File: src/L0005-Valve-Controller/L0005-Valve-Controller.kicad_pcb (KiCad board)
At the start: 4 copper layers, 101 parts, among them J1 Jumper_NO, J2 Jumper_NO, K1 AQH0223AX, K2 AQH0223AX, K3 AQH0223AX, K4 AQH0223AX, K5 AQH0223AX, K6 AQH0223AX, P1 3220-20-0200-00, P10 353620650, P11 353620650, P12 353620650, P13 353620650, P14 647676-3, P15 647676-3, P16 647676-2, P2 140-504-415-000, P3 647676-3, P4 647676-3, P5 647676-3, P6 647676-3, P7 647676-3, P8 647676-3, P9 647676-2, U1 LPC54113J256BD64QL, U2 LMS8117AMP-3.3_NOPB, U3 MAX3370EXK+T, U4 MAX3370EXK+T, U5 Optocoupler

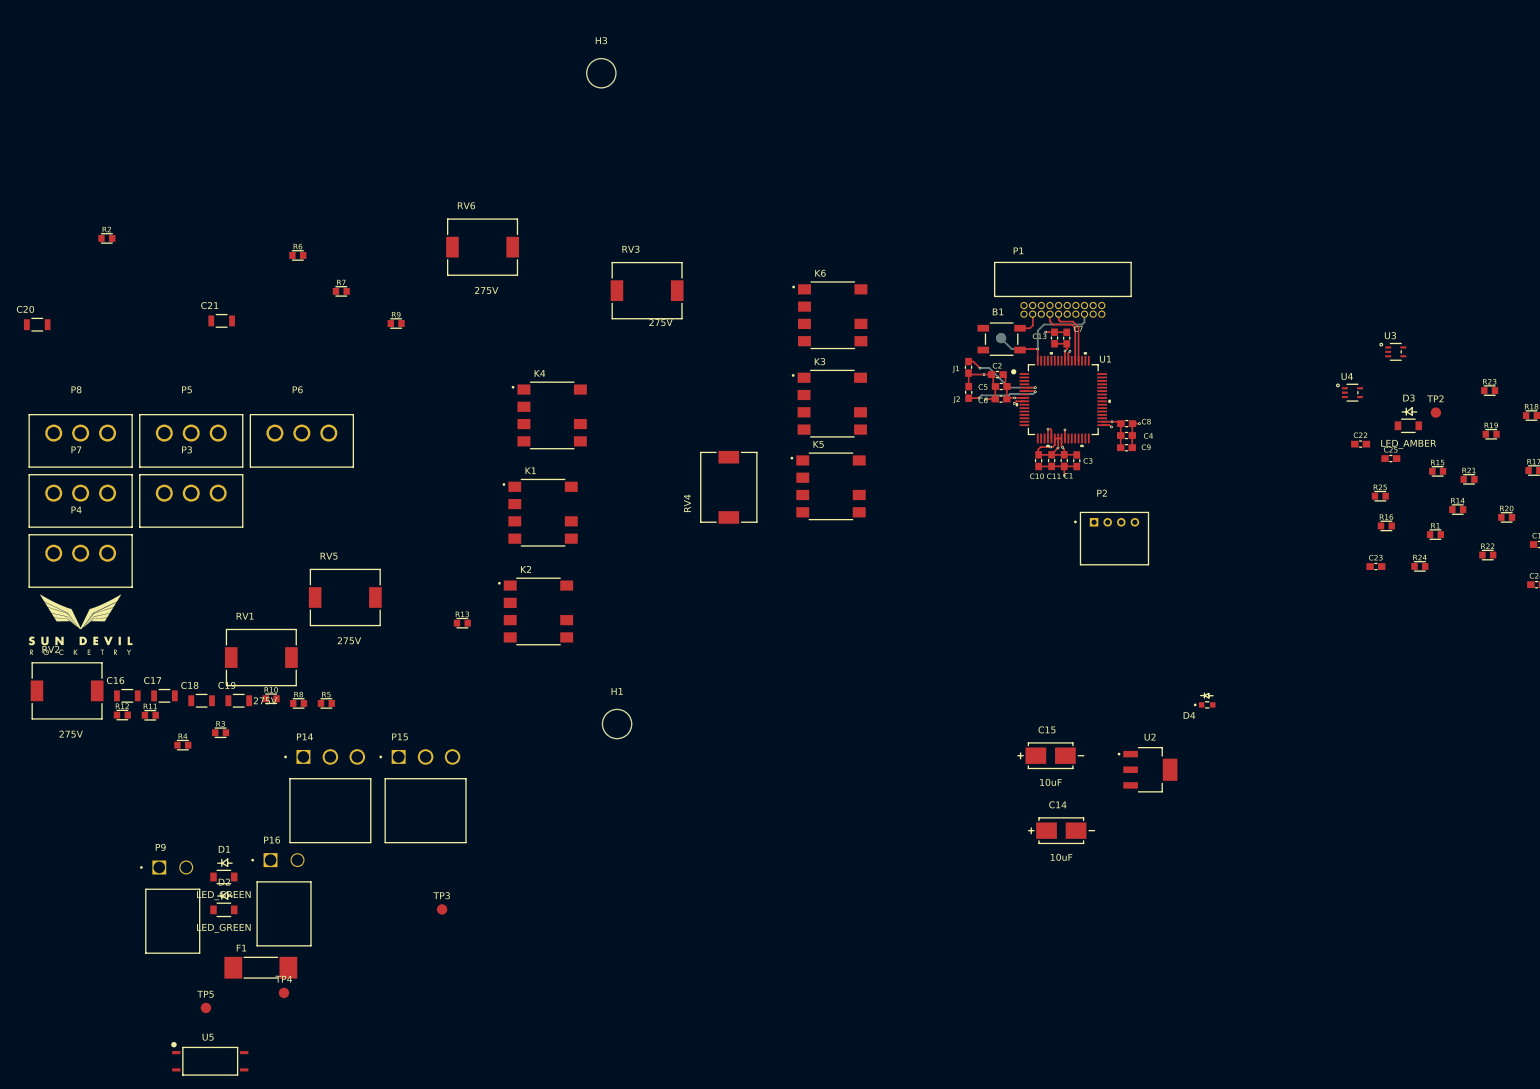
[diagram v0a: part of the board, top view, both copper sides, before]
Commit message: routed solenoid SSRs
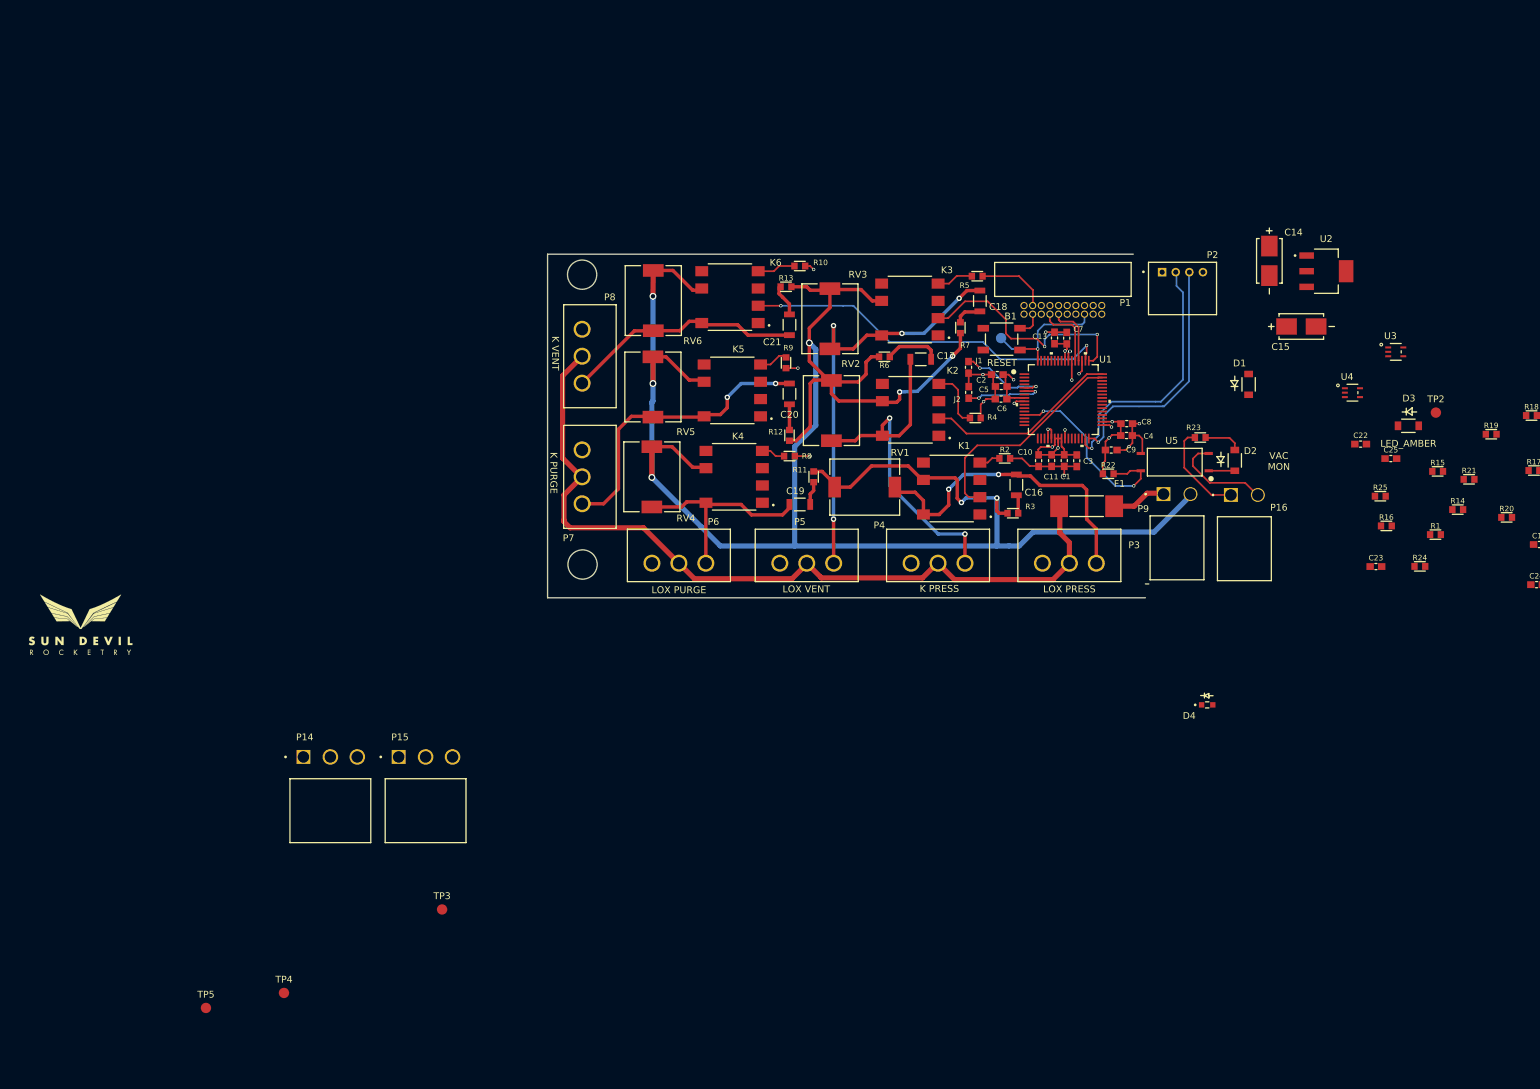
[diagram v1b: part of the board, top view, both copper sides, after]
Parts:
- moved D1 167.1 mm to (160.0, 96.1), turned to 90 degrees
- moved U5 166.9 mm to (149.1, 107.6), turned to 180 degrees
- moved D2 162.6 mm to (157.9, 107.3), turned to 90 degrees
- moved P9 157.5 mm to (147.4, 112.3)
- moved P16 151.0 mm to (157.4, 112.4)
- moved F1 139.1 mm to (136.1, 114.0)
- moved R2 135.9 mm to (124.1, 107.0)
- moved C16 134.3 mm to (125.8, 110.9), turned to 90 degrees
- moved P3 129.5 mm to (133.6, 122.4), turned to 180 degrees
- moved C18 128.6 mm to (120.4, 83.9), turned to 90 degrees
- moved P4 126.1 mm to (114.3, 122.4), turned to 180 degrees
- moved R4 126.0 mm to (119.8, 101.1)
- moved C17 121.7 mm to (111.8, 92.5), turned to 180 degrees
- moved R3 120.9 mm to (125.3, 115.1), turned to 180 degrees
- moved RV2 119.7 mm to (98.6, 100.0), turned to 90 degrees
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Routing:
- net AC_NEUTRAL: track 0.00 -> 309.0 mm, vias 0 -> 8
- net AC_HOT: track 0.00 -> 119.9 mm
- net Net-(C18-Pad2): track 0.00 -> 63.4 mm, vias 0 -> 4
- net SOL4: track 0.00 -> 54.5 mm, vias 0 -> 2
- net Net-(C17-Pad2): track 0.00 -> 53.3 mm, vias 0 -> 2
- net Net-(C16-Pad2): track 0.00 -> 46.5 mm, vias 0 -> 2
- net Net-(C20-Pad2): track 0.00 -> 44.2 mm, vias 0 -> 2
- net RX: track 0.00 -> 38.3 mm, vias 0 -> 1
- net TX: track 0.00 -> 36.6 mm, vias 0 -> 1
- net Net-(C21-Pad2): track 0.00 -> 35.0 mm
- net SOL3: track 0.00 -> 34.5 mm, vias 0 -> 2
- net SOL1: track 0.00 -> 32.7 mm
- net Net-(C19-Pad2): track 0.00 -> 31.5 mm
- net Earth: track 37.5 -> 67.0 mm, vias 10 -> 15
- net VAC_MON: track 0.00 -> 29.2 mm, vias 0 -> 2
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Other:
- board outline added: 88.4 x 50.5 mm
- board text added: "K PRESS"
- board text added: "K PURGE"
- board text added: "K VENT"
- board text added: "LOX PRESS"
- board text added: "LOX PURGE"
- board text added: "LOX VENT"
- board text added: "RESET"
- board text added: "VAC MON"

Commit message: finished controller routing
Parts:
- removed H2: Mounting-Hole, L0005-Valve-Controller:MountingHole_4.3mm_M4_DIN965
- TP2, TP3, TP4, TP5: moved to B.Cu
- moved LOGO1 185.1 mm to (172.2, 110.7)
- moved P14 166.9 mm to (177.3, 92.3), turned to 180 degrees
- moved P15 158.5 mm to (183.5, 95.5), turned to 90 degrees
- moved TP5 157.8 mm to (142.3, 107.2)
- moved TP3 149.5 mm to (161.7, 84.6)
- moved TP4 144.2 mm to (139.2, 107.2)
- moved D4 57.3 mm to (142.4, 87.1), turned to 180 degrees
- moved C12 55.2 mm to (164.1, 80.2)
- moved H4 54.9 mm to (191.9, 80.8)
- moved R24 49.7 mm to (147.9, 90.0)
- moved P10 48.3 mm to (173.2, 122.6)
- moved C24 48.2 mm to (163.2, 97.4), turned to 270 degrees
- moved R1 47.2 mm to (159.6, 80.1)
- moved P11 41.4 mm to (190.3, 122.7)
- moved D3 40.5 mm to (144.1, 92.6), turned to 180 degrees
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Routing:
- net 5V: track 0.00 -> 201.9 mm
- net Earth: track 67.0 -> 151.6 mm, vias 15 -> 23
- net ~SBV2_EN: track 0.00 -> 78.1 mm, vias 0 -> 1
- net ~SBV2_DIR: track 0.00 -> 73.4 mm, vias 0 -> 4
- net PG1: track 0.00 -> 68.5 mm, vias 0 -> 2
- net PG2: track 0.00 -> 66.6 mm, vias 0 -> 3
- net SOL6: track 2.45 -> 61.3 mm, vias 1 -> 2
- net SOL5: track 2.08 -> 56.3 mm, vias 1 -> 2
- net ~SBV1_EN: track 0.00 -> 51.1 mm
- net ~SBV1_DIR: track 0.00 -> 49.7 mm, vias 0 -> 1
- net ENCD1_A: track 0.00 -> 45.5 mm, vias 0 -> 2
- net ENCD2_A: track 0.00 -> 44.0 mm, vias 0 -> 2
- net 3.3V: track 39.8 -> 81.5 mm, vias 6 -> 10
- net /SBV2_PUL5: track 0.00 -> 40.2 mm, vias 0 -> 2
- net ENCD2_B: track 0.00 -> 37.1 mm, vias 0 -> 2
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- added copper zone on In2.Cu, net 3.3V
- added copper zone on In1.Cu, net Earth
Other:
- board size 88.4 x 50.5 mm -> 141.7 x 50.5 mm
- board text added: "AC MON"
- board text added: "AC POWER"
- board text added: "EXCEPT"
- board text added: "K ENCODER"
- board text added: "K MAIN"
- board text added: "K PG"
- board text added: "L0005 Revision 1.0"
- board text added: "LOX ENCODER"
- board text added: "LOX MAIN"
- board text added: "LOX PG"
- board text added: "POWER"
- board text added: "STATUS"

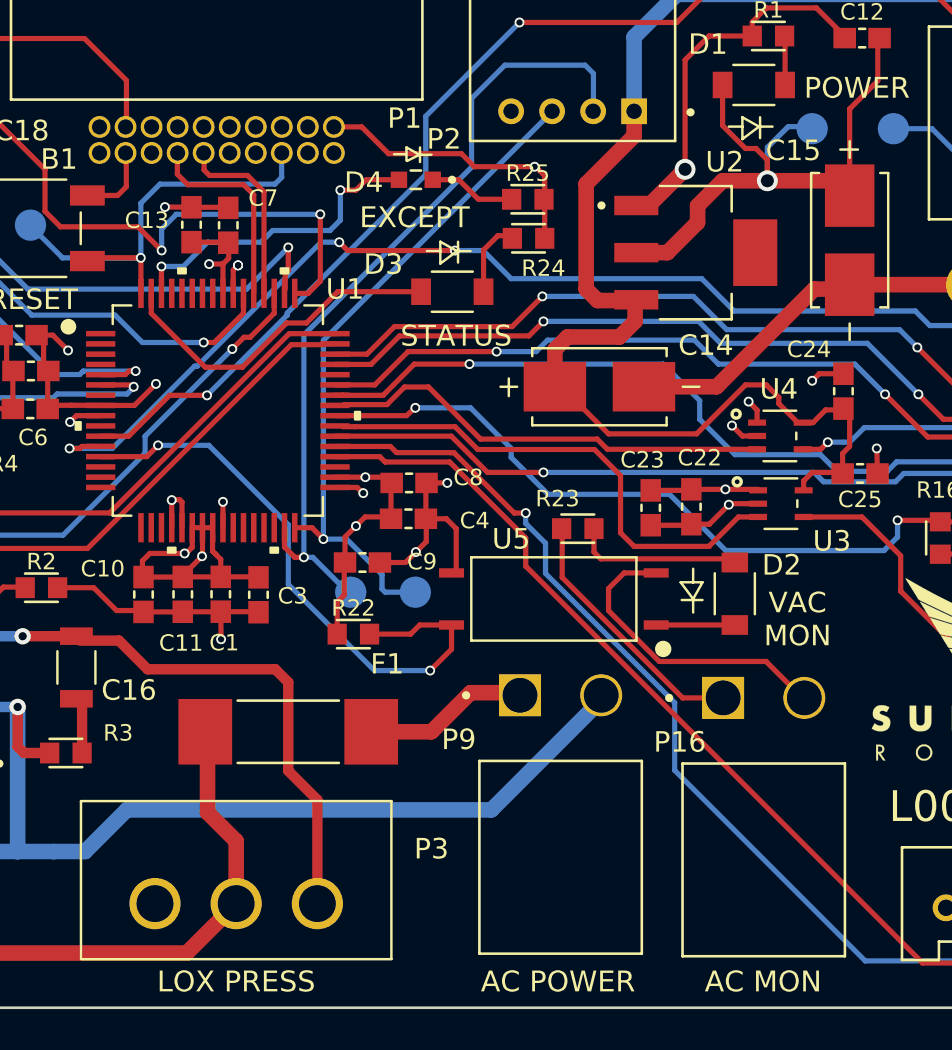
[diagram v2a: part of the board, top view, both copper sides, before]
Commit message: fixed SWD schematic connections for J-Link
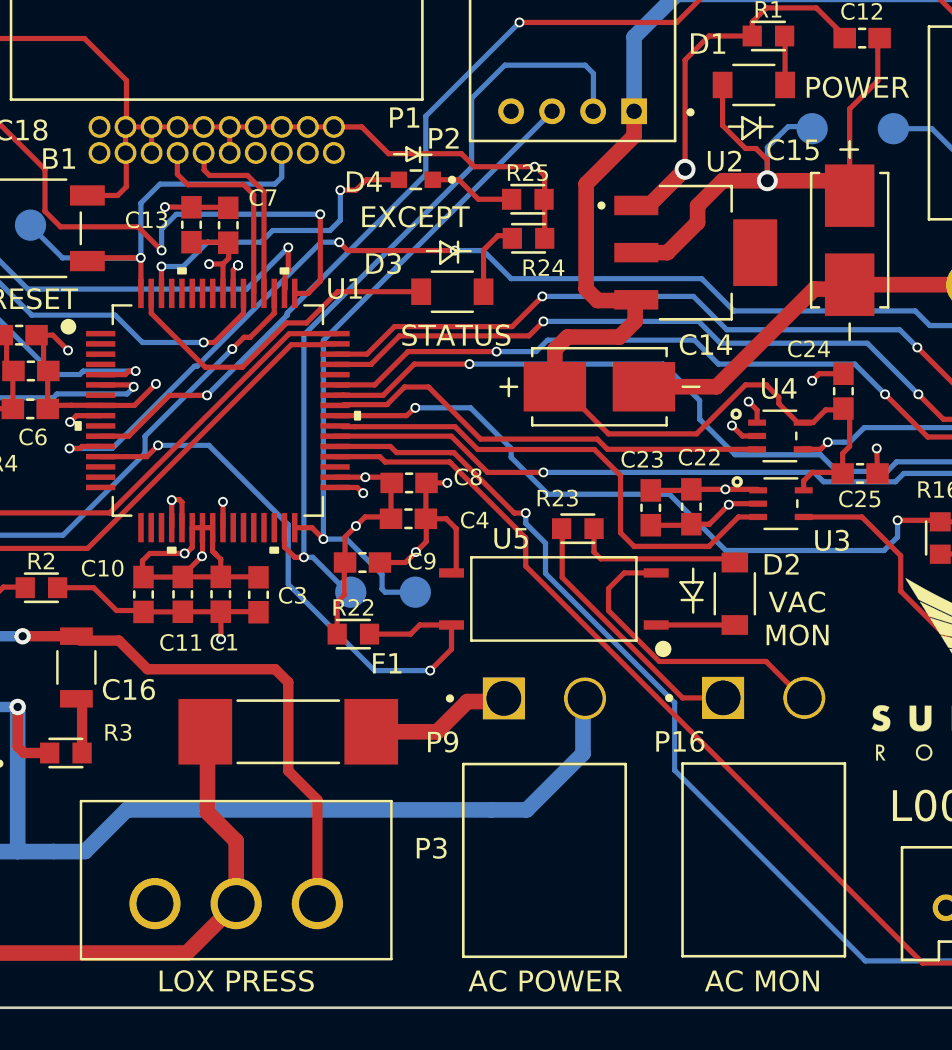
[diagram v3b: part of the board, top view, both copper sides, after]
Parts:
- moved P9 0.80 mm to (146.7, 112.4)
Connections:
- net ~SBV1_DIR renamed ~{SBV1_DIR}
- net ~SBV1_EN renamed ~{SBV1_EN}
- net ~SBV2_DIR renamed ~{SBV2_DIR}
- net ~SBV2_EN renamed ~{SBV2_EN}
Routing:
- net Earth: track 151.6 -> 165.5 mm
- net Net-(F1-Pad2): track 8.17 -> 7.03 mm
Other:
- net class Default removed
